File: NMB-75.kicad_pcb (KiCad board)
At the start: 2 copper layers, 72.1 x 38.1 mm, 24 parts, among them SW1 SW_Push, U1 ATmega32U4-AU, Y1 16MHz

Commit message: working on traces
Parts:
- USB1: moved to F.Cu
- moved F1 8.43 mm to (46.9, 58.3)
- moved R2 5.25 mm to (39.2, 58.5)
- moved C6 3.40 mm to (62.4, 60.2), turned to 270 degrees
- moved R4 3.37 mm to (66.8, 60.3), turned to 270 degrees
- moved R3 1.76 mm to (43.3, 58.3), turned to 90 degrees
- moved C4 0.56 mm to (66.2, 70.8)
- moved USB1 0.38 mm to (41.8, 48.6)
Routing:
- net GND: track 0.00 -> 9.45 mm
- net VCC: track 0.00 -> 5.20 mm
- net D+: track 0.00 -> 5.06 mm
- net D-: track 0.00 -> 4.63 mm

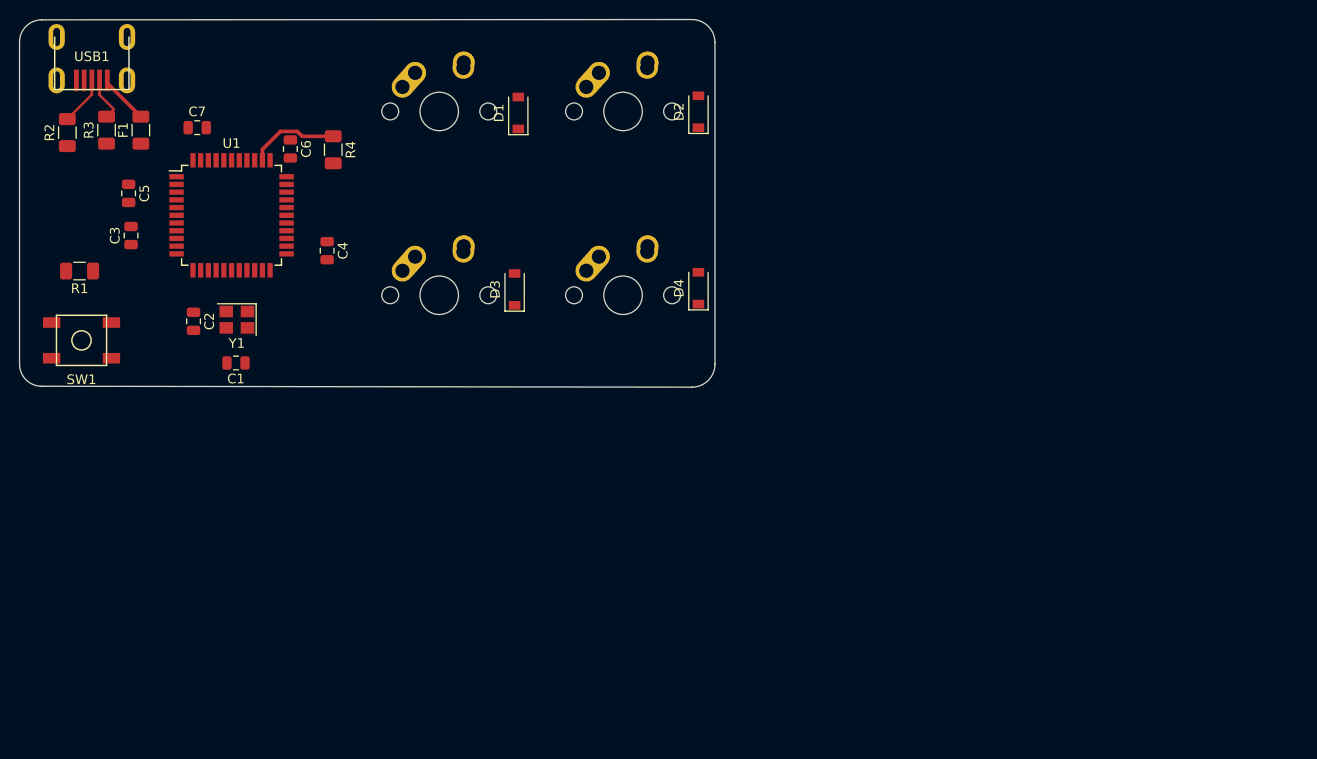
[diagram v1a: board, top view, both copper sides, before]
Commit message: routing finished on learning board
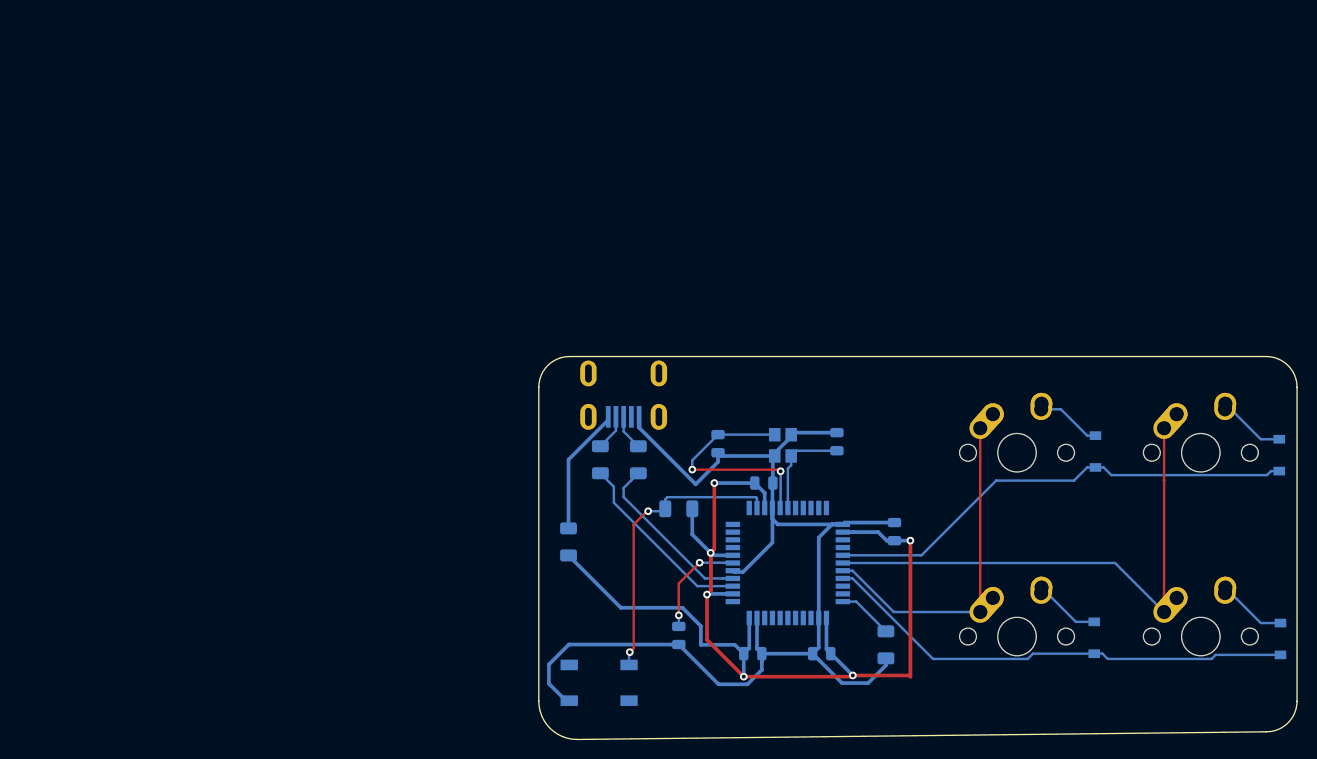
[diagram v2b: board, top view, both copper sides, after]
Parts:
- C1, C2, C3, C4, C5, C6, C7, D1, D2, D3, D4, F1, R1, R2, R3, R4, SW1, U1, USB1, Y1: moved to B.Cu
- moved C5 86.2 mm to (117.4, 112.6), turned to 180 degrees
- moved C7 79.3 mm to (110.3, 112.6)
- moved R4 76.9 mm to (124.1, 111.6), turned to 90 degrees
- moved C6 74.1 mm to (125.0, 99.9), turned to 90 degrees
- moved D4 70.4 mm to (165.0, 111.0)
- moved C3 70.3 mm to (102.6, 110.7), turned to 270 degrees
- moved D3 70.1 mm to (145.7, 110.9)
- moved D2 69.9 mm to (164.8, 92.0)
- moved MX1 69.5 mm to (137.7, 91.7)
- moved MX3 69.5 mm to (137.7, 110.8)
- moved MX2 69.5 mm to (156.7, 91.7)
- moved MX4 69.5 mm to (156.7, 110.8)
- moved D1 69.3 mm to (145.8, 91.6)
- moved R2 68.2 mm to (98.4, 92.5)
- moved U1 68.0 mm to (113.9, 103.2)
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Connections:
- U1 pad 27: Net-(U1-Pad27) -> ROW0
- U1 pad 28: Net-(U1-Pad28) -> COL1
- U1 pad 29: Net-(U1-Pad29) -> COL0
- U1 pad 30: Net-(U1-Pad30) -> ROW1
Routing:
- net +5V: track 0.00 -> 115.4 mm, vias 0 -> 6
- net GND: track 9.45 -> 122.6 mm
- net COL1: track 0.00 -> 54.6 mm
- net ROW0: track 0.00 -> 49.5 mm
- net ROW1: track 0.00 -> 49.4 mm
- net COL0: track 0.00 -> 35.1 mm
- net Net-(R1-Pad2): track 0.00 -> 30.3 mm, vias 0 -> 2
- net Net-(C2-Pad1): track 0.00 -> 23.7 mm, vias 0 -> 2
- net Net-(R3-Pad1): track 0.00 -> 19.5 mm
- net Net-(R2-Pad1): track 0.00 -> 17.9 mm
- net Net-(C3-Pad1): track 0.00 -> 11.0 mm, vias 0 -> 2
- net Net-(C1-Pad1): track 0.00 -> 10.5 mm
- net VCC: track 5.20 -> 13.3 mm
- net Net-(D4-Pad2): track 0.00 -> 7.24 mm
- net Net-(D2-Pad2): track 0.00 -> 7.11 mm
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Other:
- board outline removed

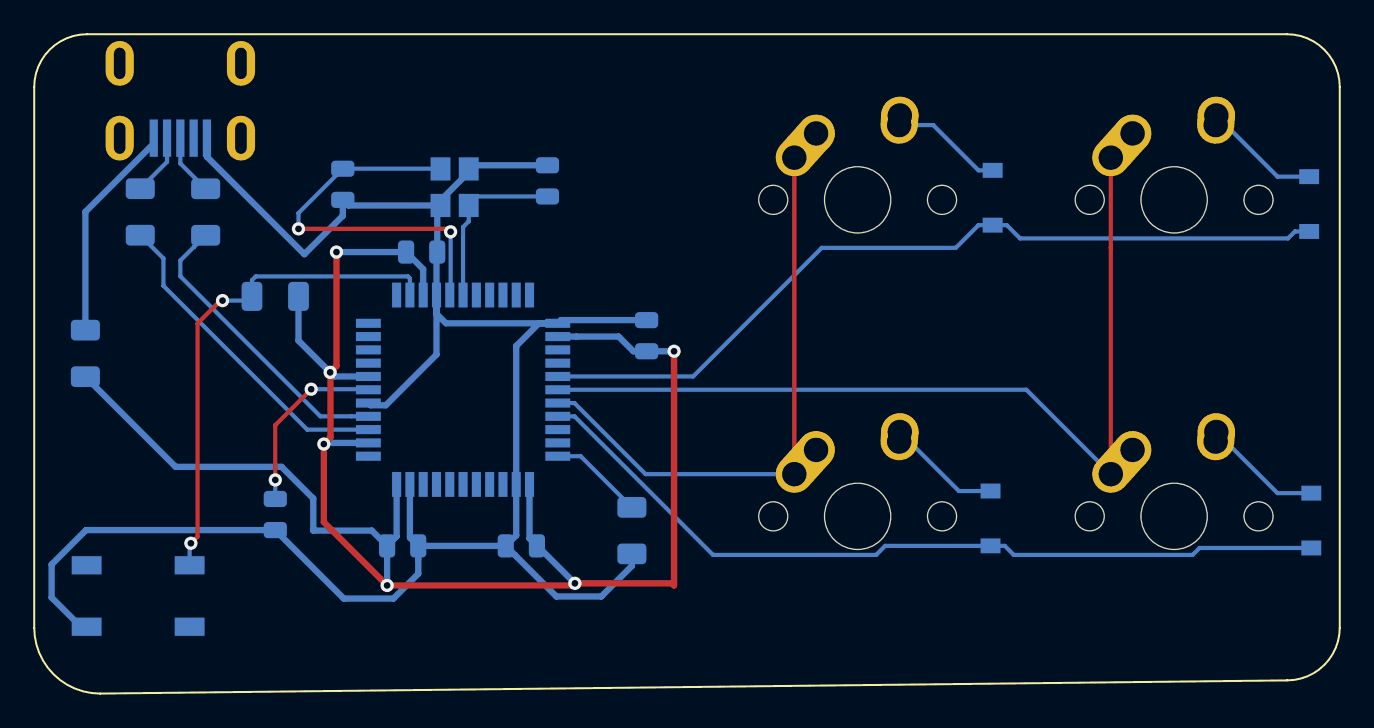
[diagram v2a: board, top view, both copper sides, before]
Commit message: Added ground fill, decor text and generated gerbers
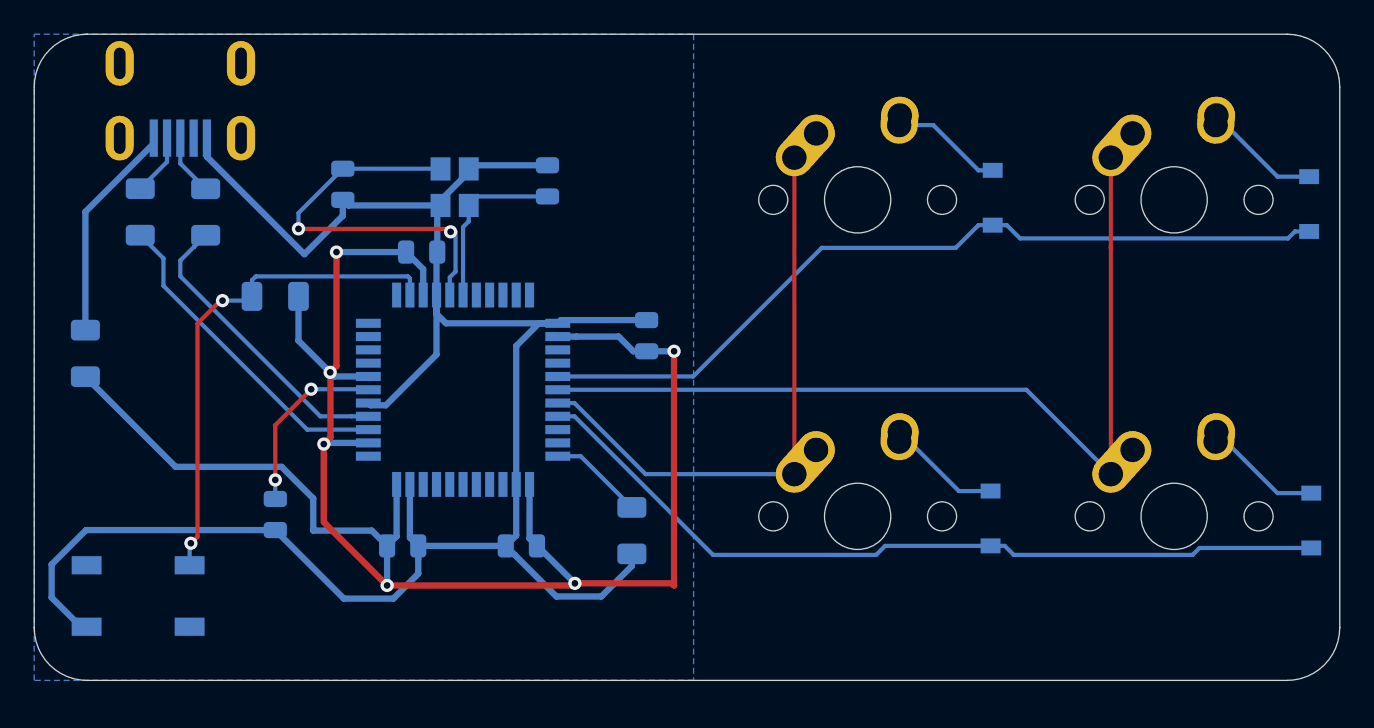
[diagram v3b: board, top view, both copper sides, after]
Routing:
- added copper zone on B.Cu, net GND
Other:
- board outline added: 78.6 x 38.9 mm
- board text added: "æ"
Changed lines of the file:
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@@
   (general
     (thickness 1.6)
-    (drawings 8)
-    (tracks 190)
+    (drawings 9)
+    (tracks 194)
     (zones 0)
     (modules 24)
@@
     (39 F.Mask user)
     (40 Dwgs.User user)
-    (41 Cmts.User user)
+    (41 Cmts.User user hide)
     (42 Eco1.User user)
     (43 Eco2.User user)
@@
     )
   )
-  (gr_line (start 163.5125 120.65) (end 92.075 121.44375) (layer F.SilkS) (width 0.12))
-  (gr_line (start 166.6875 84.93125) (end 166.6875 117.475) (layer F.SilkS) (width 0.12))
-  (gr_line (start 91.28125 81.75625) (end 163.5125 81.75625) (layer F.SilkS) (width 0.12))
-  (gr_line (start 88.10625 84.93125) (end 88.10625 117.475) (layer F.SilkS) (width 0.12))
-  (gr_arc (start 92.075 117.475) (end 88.10625 117.475) (angle -90) (layer F.SilkS) (width 0.12))
-  (gr_arc (start 91.28125 84.93125) (end 91.28125 81.75625) (angle -90) (layer F.SilkS) (width 0.12))
-  (gr_arc (start 163.5125 117.475) (end 163.5125 120.65) (angle -90) (layer F.SilkS) (width 0.12))
-  (gr_arc (start 163.5125 84.93125) (end 166.6875 84.93125) (angle -90) (layer F.SilkS) (width 0.12))
+  (gr_text æ (at 111.125 117.475) (layer B.SilkS)
+    (effects (font (size 2.54 2.54) (thickness 0.15)) (justify mirror))
+  )
+  (gr_line (start 166.6875 84.93125) (end 166.6875 117.475) (layer Edge.Cuts) (width 0.05))
+  (gr_line (start 91.28125 81.75625) (end 163.5125 81.75625) (layer Edge.Cuts) (width 0.05))
+  (gr_line (start 91.28125 120.65) (end 163.5125 120.65) (layer Edge.Cuts) (width 0.05))
+  (gr_line (start 88.10625 117.475) (end 88.10625 84.93125) (layer Edge.Cuts) (width 0.05))
+  (gr_arc (start 91.28125 84.93125) (end 91.28125 81.75625) (angle -90) (layer Edge.Cuts) (width 0.05))
+  (gr_arc (start 91.28125 117.475) (end 88.10625 117.475) (angle -90) (layer Edge.Cuts) (width 0.05))
+  (gr_arc (start 163.5125 117.475) (end 163.5125 120.65) (angle -90) (layer Edge.Cuts) (width 0.05))
+  (gr_arc (start 163.5125 84.93125) (end 166.6875 84.93125) (angle -90) (layer Edge.Cuts) (width 0.05))
   (segment (start 90.911 117.42) (end 89.154 115.663) (width 0.381) (layer B.Cu) (net 1))
   (segment (start 91.261 117.42) (end 90.911 117.42) (width 0.381) (layer B.Cu) (net 1))
@@
   (segment (start 112.992865 93.472) (end 113.169823 93.648958) (width 0.254) (layer F.Cu) (net 3))
   (segment (start 113.169823 97.404927) (end 113.119 97.45575) (width 0.254) (layer B.Cu) (net 3))
-  (segment (start 113.169823 93.648958) (end 113.169823 97.404927) (width 0.254) (layer B.Cu) (net 3))
+  (segment (start 113.183365 93.6625) (end 113.169823 93.648958) (width 0.254) (layer B.Cu) (net 3))
+  (segment (start 113.46499 93.6625) (end 113.183365 93.6625) (width 0.254) (layer B.Cu) (net 3))
+  (segment (start 113.46499 96.04375) (end 113.46499 93.6625) (width 0.254) (layer B.Cu) (net 3))
+  (segment (start 113.119 97.45575) (end 113.119 96.38974) (width 0.254) (layer B.Cu) (net 3))
+  (segment (start 113.119 96.38974) (end 113.46499 96.04375) (width 0.254) (layer B.Cu) (net 3))
   (via (at 102.616 108.585) (size 0.8) (drill 0.4) (layers F.Cu B.Cu) (net 4))
   (segment (start 102.616 109.728) (end 102.616 108.585) (width 0.254) (layer B.Cu) (net 4))
@@
   (segment (start 120.99875 107.15575) (end 119.619 107.15575) (width 0.254) (layer B.Cu) (net 20))
   (segment (start 124.079 110.236) (end 120.99875 107.15575) (width 0.254) (layer B.Cu) (net 20))
+  (zone (net 1) (net_name GND) (layer B.Cu) (hatch edge 0.508)
+    (connect_pads (clearance 0.508))
+    (min_thickness 0.254)
+    (fill yes (arc_segments 32) (thermal_gap 0.508) (thermal_bridge_width 0.508))
+    (polygon
+      (pts
+        (xy 88.10625 81.75625) (xy 127.79375 81.75625) (xy 127.79375 120.65) (xy 88.10625 120.65)
+      )
+    )
+  )
 )
